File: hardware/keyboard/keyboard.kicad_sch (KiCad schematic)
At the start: 13 parts, among them J1 Conn_01x02_Female, J2 Conn_01x03_Female, Q1 Q_NMOS_SGD, SW1 SW_Push, U1 SC0915, U2 MCP23008-xP

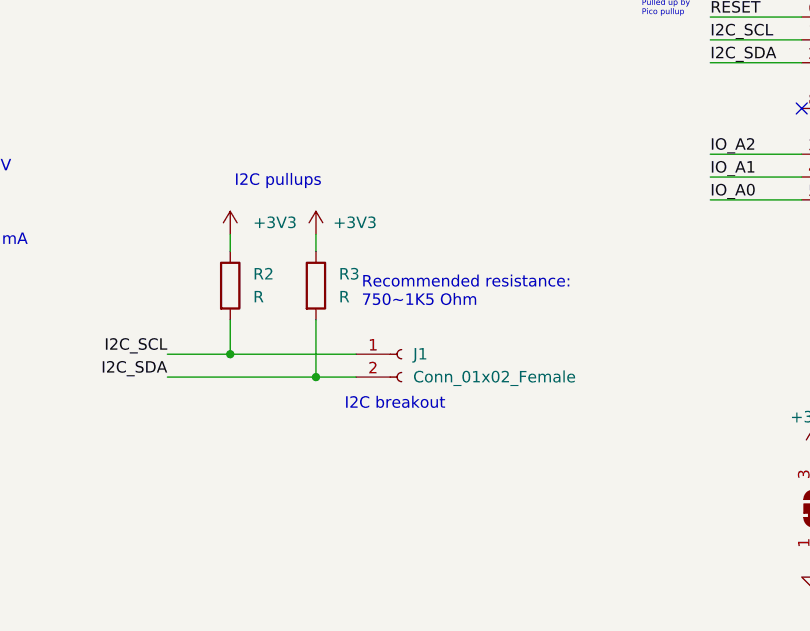
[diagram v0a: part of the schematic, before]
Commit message: Update I2C header
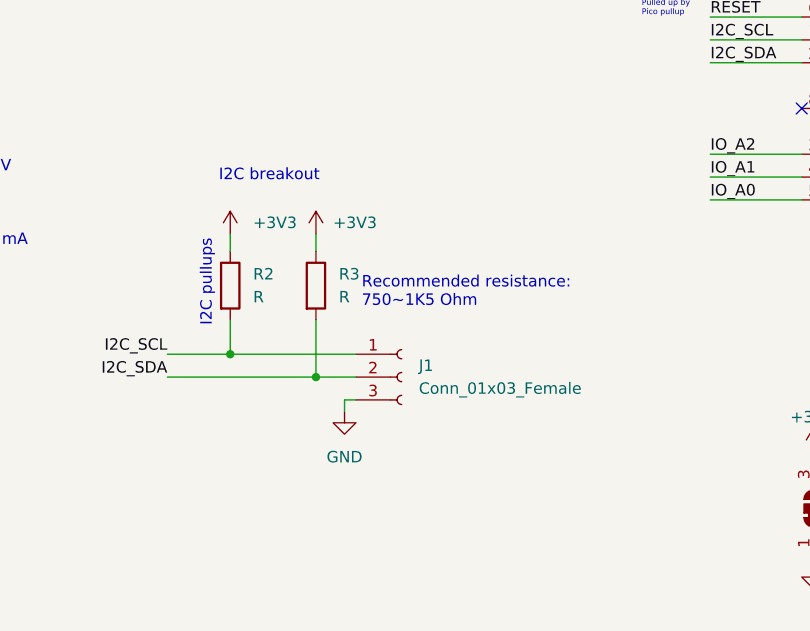
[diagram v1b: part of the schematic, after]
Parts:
- removed J1: Conn_01x02_Female, Connector_PinHeader_2.54mm:PinHeader_1x02_P2.54mm_Vertical, symbol Connector:Conn_01x02_Female
- added J1: Conn_01x03_Female, Connector_PinSocket_2.54mm:PinSocket_1x03_P2.54mm_Vertical, symbol Connector:Conn_01x03_Female
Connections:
- net GND: now also J1.3 (Pin_3)
- net I2C_SCL: now also J1.1 (Pin_1)
- net I2C_SDA: now also J1.2 (Pin_2)
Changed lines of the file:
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@@
     (stroke (width 0) (type default) (color 0 0 0 0))
   )
+  (wire (pts (xy 295.275 92.075) (xy 294.005 92.075))
+    (stroke (width 0) (type default) (color 0 0 0 0))
+  )
   (wire (pts (xy 218.44 194.945) (xy 227.33 194.945))
     (stroke (width 0) (type default) (color 0 0 0 0))
@@
     (stroke (width 0) (type default) (color 0 0 0 0))
   )
+  (wire (pts (xy 294.005 92.075) (xy 294.005 93.345))
+    (stroke (width 0) (type default) (color 0 0 0 0))
+  )
   (wire (pts (xy 104.14 216.535) (xy 113.03 216.535))
     (stroke (width 0) (type default) (color 0 0 0 0))
@@
     (effects (font (size 0.635 0.635)) (justify left bottom))
   )
-  (text "I2C pullups" (at 291.465 68.58 180)
+  (text "I2C pullups" (at 279.4 74.295 270)
     (effects (font (size 1.27 1.27)) (justify right bottom))
   )
@@
     (effects (font (size 1.27 1.27)) (justify left bottom))
   )
-  (text "I2C breakout" (at 294.005 93.345 0)
+  (text "I2C breakout" (at 280.035 67.945 0)
     (effects (font (size 1.27 1.27)) (justify left bottom))
   )
@@
     (pin "1")
   )
+  (symbol (lib_id "power:GND") (at 294.005 93.345 0) (unit 1)
+    (in_bom yes) (on_board yes) (fields_autoplaced)
+    (property "Reference" "#PWR0186" (id 0) (at 294.005 99.695 0)
+      (effects (font (size 1.27 1.27)) hide)
+    )
+    (property "Value" "GND" (id 1) (at 294.005 98.425 0))
+    (property "Footprint" "" (id 2) (at 294.005 93.345 0)
+      (effects (font (size 1.27 1.27)) hide)
+    )
+    (property "Datasheet" "" (id 3) (at 294.005 93.345 0)
+      (effects (font (size 1.27 1.27)) hide)
+    )
+    (pin "1")
+  )
   (symbol (lib_id "power:+5V") (at 194.31 211.455 270) (unit 1)
     (in_bom yes) (on_board yes)
@@
     (pin "2")
   )
-  (symbol (lib_id "Connector:Conn_01x02_Female") (at 300.355 86.995 0) (unit 1)
+  (symbol (lib_id "Connector:Conn_01x03_Female") (at 300.355 89.535 0) (unit 1)
     (in_bom yes) (on_board yes) (fields_autoplaced)
-    (property "Reference" "J1" (id 0) (at 301.625 86.9949 0)
+    (property "Reference" "J1" (id 0) (at 302.26 88.2649 0)
       (effects (font (size 1.27 1.27)) (justify left))
     )
-    (property "Value" "Conn_01x02_Female" (id 1) (at 301.625 89.5349 0)
+    (property "Value" "Conn_01x03_Female" (id 1) (at 302.26 90.8049 0)
       (effects (font (size 1.27 1.27)) (justify left))
     )
-    (property "Footprint" "Connector_PinHeader_2.54mm:PinHeader_1x02_P2.54mm_Vertical" (id 2) (at 300.355 86.995 0)
+    (property "Footprint" "Connector_PinSocket_2.54mm:PinSocket_1x03_P2.54mm_Vertical" (id 2) (at 300.355 89.535 0)
       (effects (font (size 1.27 1.27)) hide)
     )
-    (property "Datasheet" "~" (id 3) (at 300.355 86.995 0)
+    (property "Datasheet" "~" (id 3) (at 300.355 89.535 0)
       (effects (font (size 1.27 1.27)) hide)
     )
     (pin "1")
     (pin "2")
+    (pin "3")
   )
   (symbol (lib_id "Device:R") (at 281.305 79.375 0) (unit 1)
@@
       (reference "#PWR0185") (unit 1) (value "GND") (footprint "")
     )
-    (path "/ea927ece-599f-4dc5-8a96-3344d28cc9f7"
-      (reference "J1") (unit 1) (value "Conn_01x02_Female") (footprint "Connector_PinHeader_2.54mm:PinHeader_1x02_P2.54mm_Vertical")
+    (path "/835b9234-b9bb-4bad-aa16-fabd3ea9df4a"
+      (reference "#PWR0186") (unit 1) (value "GND") (footprint "")
+    )
+    (path "/ea09115f-9b7c-45a4-93f0-a006cf15a4d7"
+      (reference "J1") (unit 1) (value "Conn_01x03_Female") (footprint "Connector_PinSocket_2.54mm:PinSocket_1x03_P2.54mm_Vertical")
     )
     (path "/56cbf55b-440b-4f93-b0a7-87799c7707ad"

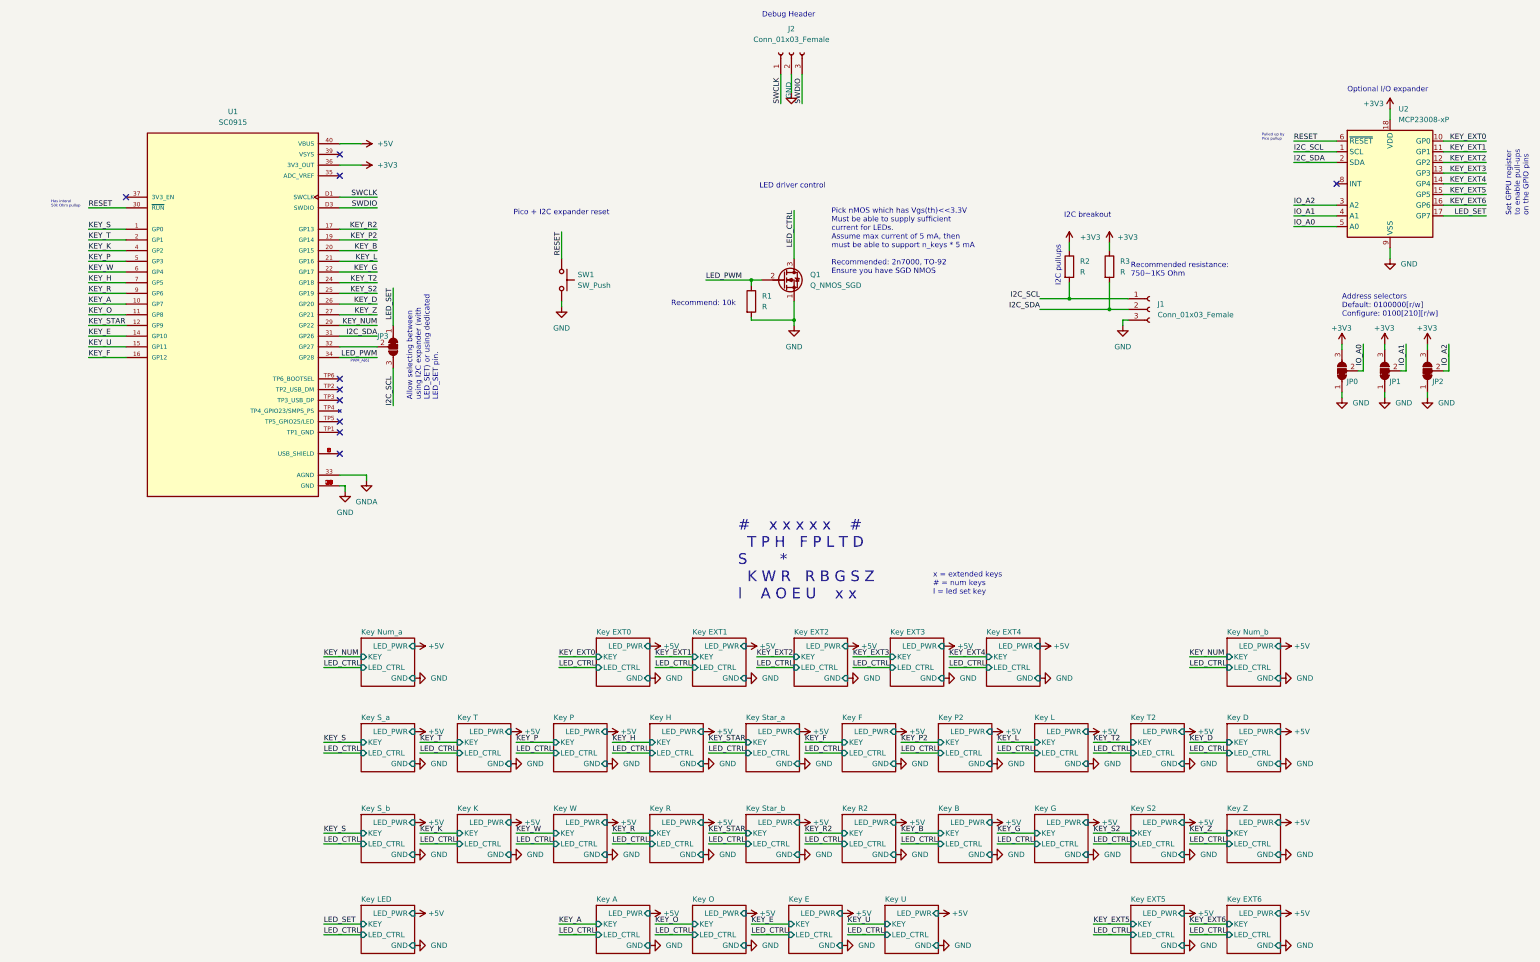
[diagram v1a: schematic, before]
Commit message: Add mounting holes
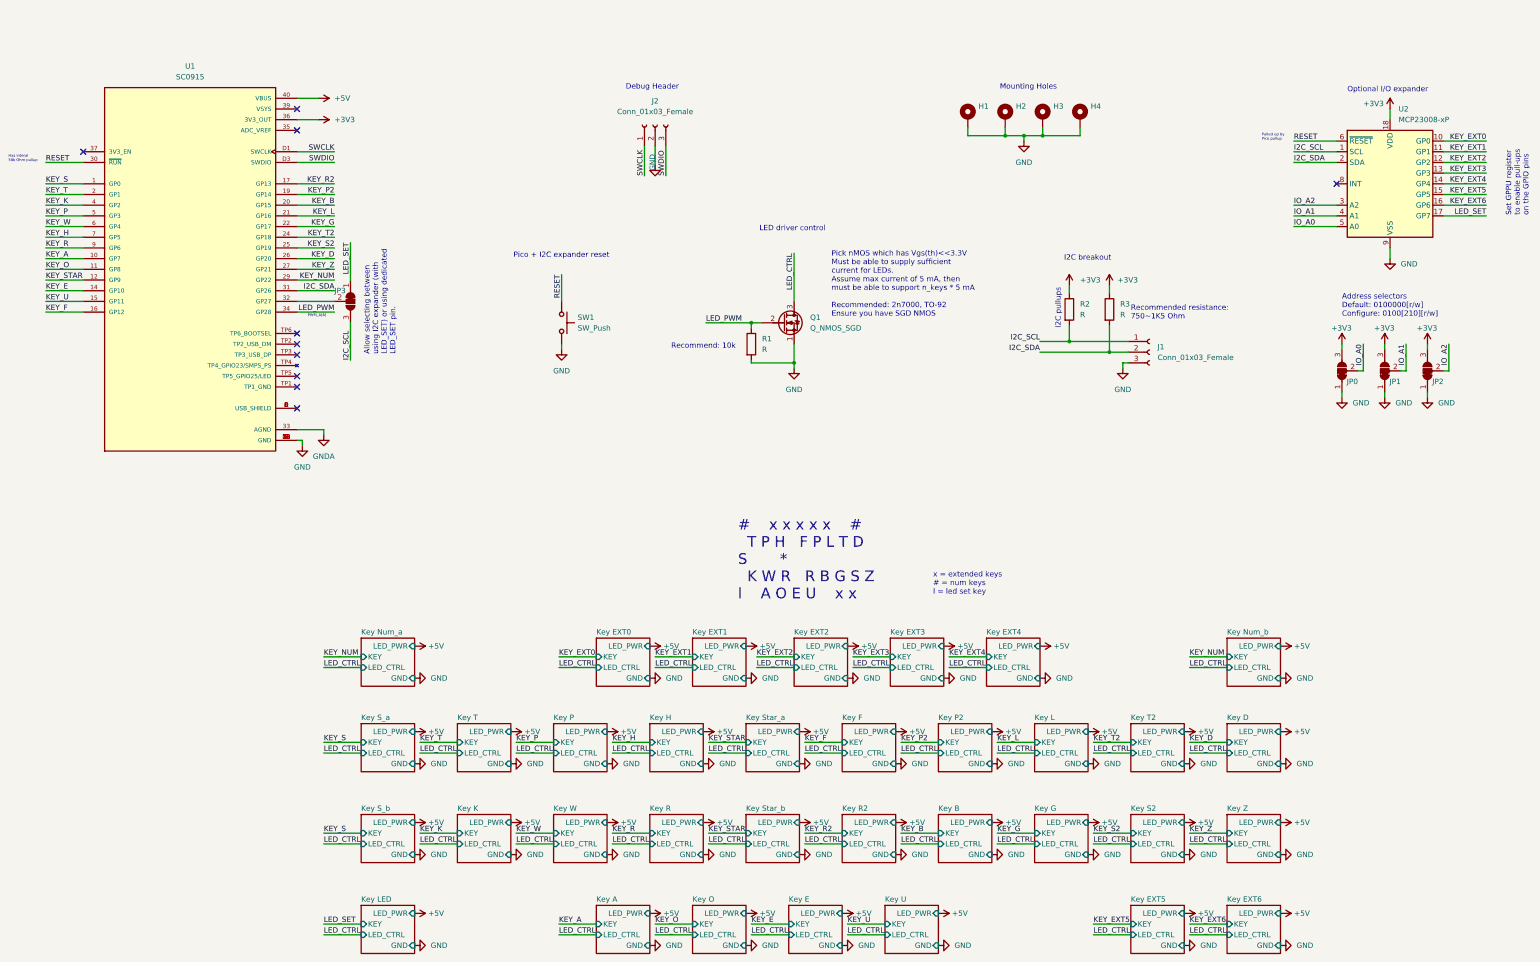
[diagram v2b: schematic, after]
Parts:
- added H1, H2, H3, H4: MountingHole_Pad, MountingHole:MountingHole_3mm_Pad_Via, symbol Mechanical:MountingHole_Pad
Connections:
- net GND: now also H1.1, H2.1, H3.1, H4.1
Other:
- note added: "Mounting Holes"
- moved on the sheet: J1, J2, JP3, Q1, R1, R2, R3, SW1, U1
